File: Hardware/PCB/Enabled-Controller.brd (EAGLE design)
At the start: 54 x 71 mm, 14 parts, among them U1 ITSYBITSY

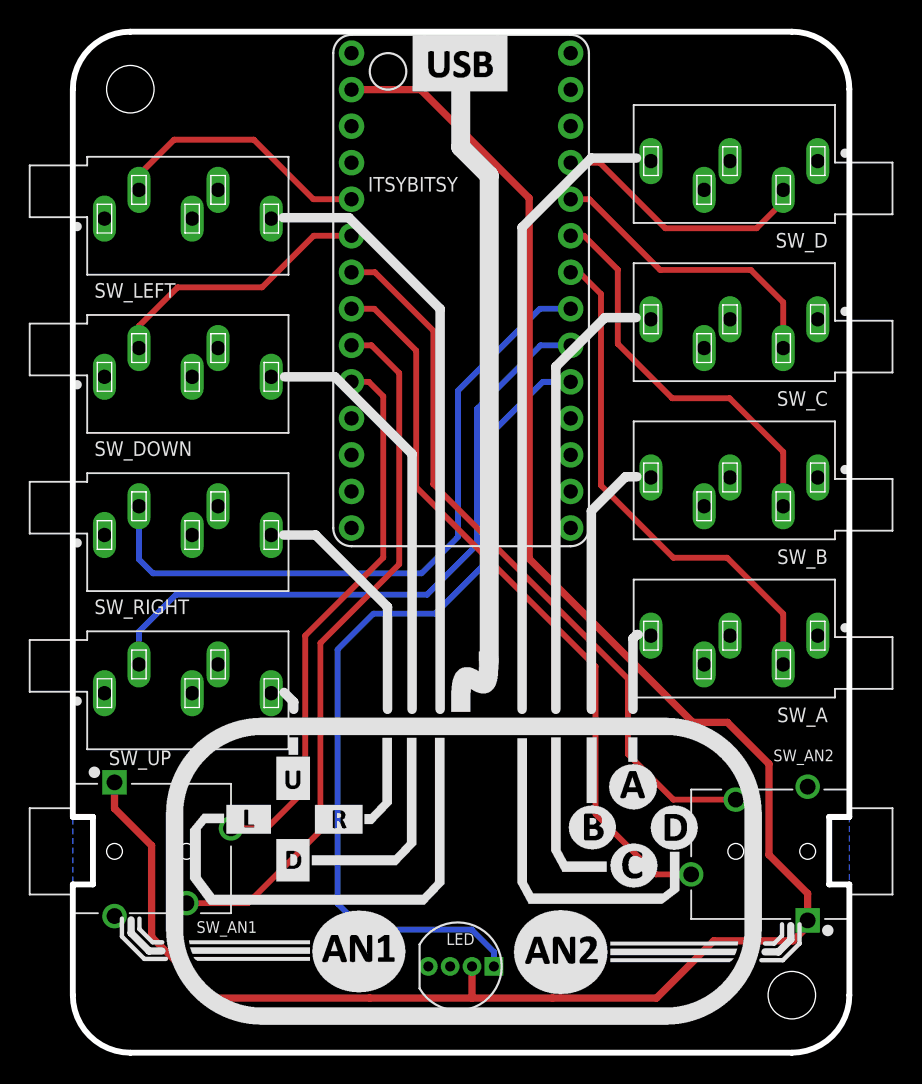
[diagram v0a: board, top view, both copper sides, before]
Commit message: Updated Eagle files
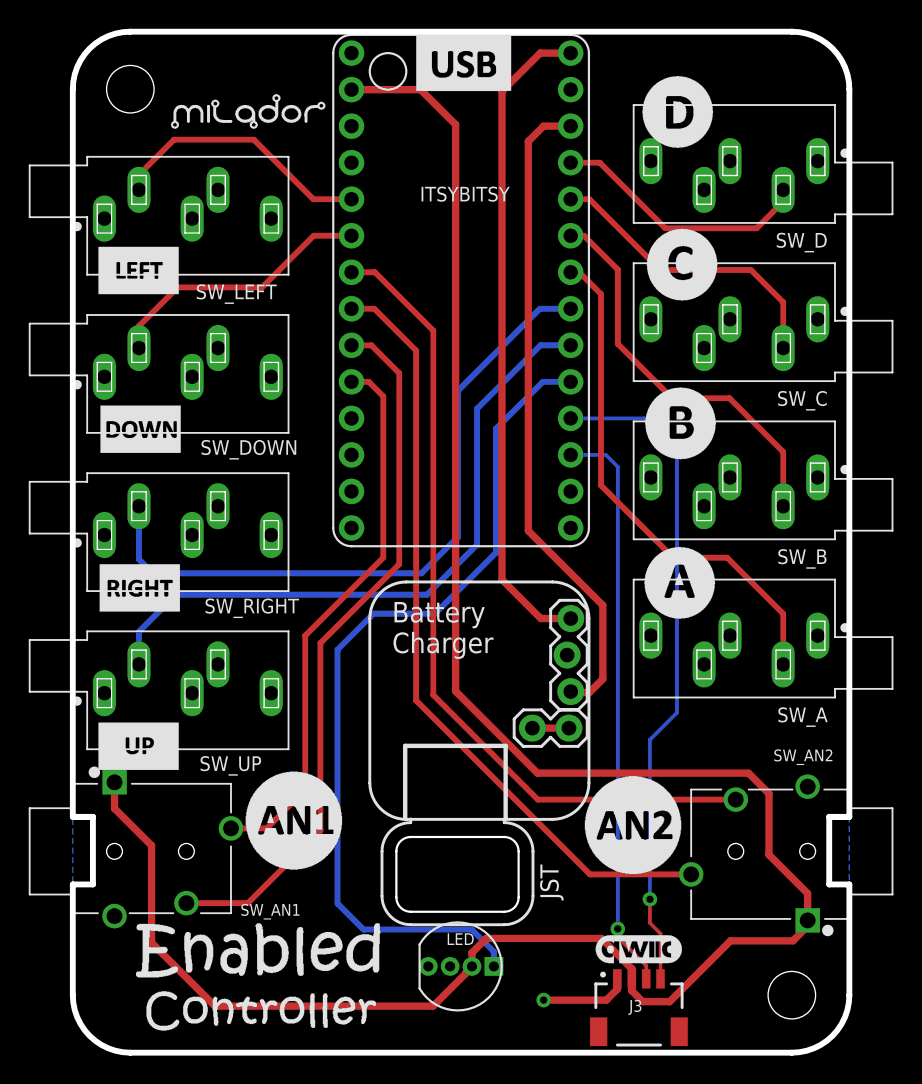
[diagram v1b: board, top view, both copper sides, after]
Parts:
- added J1: (no value), milador:HEADER_FEMALE-1X03_LONGER
- added J2: HEADER_FEMALE-1X2, milador:HEADER_FEMALE-1X02
- added J3: QWIIC, milador_SMD:CONNECTORS_JST04_1MM_RA
- added U$1: MILADOR-LOGO-, milador:MILADOR_LOGO1
- added U$21: (no value), SparkFun-Aesthetics:QWIIC_6MM
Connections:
- new net N$14: J3.4, U1.P_SCL
- new net N$15: J3.3, U1.P_SDA
- new net N$16: J1.3, U1.P_USB
- new net N$17: J1.1, U1.P_BAT
- new net N$18: J2.1, J2.2
- net +3V3: now also J3.2
- net GND: now also J3.1
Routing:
- net N$14: track 0.00 -> 46.1 mm, vias 0 -> 1
- net N$17: track 0.00 -> 45.7 mm
- net N$16: track 0.00 -> 45.6 mm
- net N$15: track 0.00 -> 40.0 mm, vias 0 -> 1
- net +3V3: track 139.0 -> 149.8 mm
- net GND: track 0.00 -> 6.16 mm, vias 0 -> 1
- net N$12: track 51.2 -> 56.8 mm
- net N$9: track 51.5 -> 54.2 mm
- net N$18: track 0.00 -> 2.54 mm
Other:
- outline, holes or cut-outs redrawn
- board text added: "Battery Charger"
- board text added: "JST"

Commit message: Added updated PCB files
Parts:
- removed J2: HEADER_FEMALE-1X2, milador:HEADER_FEMALE-1X02
- removed U$1: MILADOR-LOGO-, milador:MILADOR_LOGO1
- added LABEL1: MILADOR-LOGO-, milador:MILADOR_LOGO1
- renumbered U$21 to LABEL2
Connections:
- removed net N$18: J2.1, J2.2
- net GND: now also J1.2, SW_A.3, SW_B.3, SW_C.3, SW_D.3, SW_DOWN.3, SW_LEFT.3, SW_RIGHT.3, SW_UP.3
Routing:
- net N$18: track 2.54 -> 0.00 mm
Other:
- board text added: "V1.2"
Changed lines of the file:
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@@
 <drawing>
 <settings>
-<setting alwaysvectorfont="yes"/>
+<setting alwaysvectorfont="no"/>
 <setting keepoldvectorfont="yes"/>
 <setting verticaltext="up"/>
@@
 <layer number="20" name="Dimension" color="15" fill="1" visible="yes" active="yes"/>
 <layer number="21" name="tPlace" color="7" fill="1" visible="yes" active="yes"/>
-<layer number="22" name="bPlace" color="7" fill="1" visible="yes" active="yes"/>
+<layer number="22" name="bPlace" color="7" fill="1" visible="no" active="yes"/>
 <layer number="23" name="tOrigins" color="15" fill="1" visible="yes" active="yes"/>
 <layer number="24" name="bOrigins" color="15" fill="1" visible="yes" active="yes"/>
@@
 </layers>
 <board>
-<fusionsync huburn="a.cGVyc29uYWw6dWUyYWQxOTI2" projecturn="a.cGVyc29uYWw6dWUyYWQxOTI2IzIwMjAwODAxMzIwMTk3MTgx" f3durn="urn:adsk.wipprod:dm.lineage:0P3WCUaEQdKCa3VO5MvKcA" pcbguid="" lastpulledtime="" lastsyncedchangeguid="" latestrevisionid="d0e29ba4-d4c4-4277-8ff9-67c412f5de14" lastsyncedrevisionid="d0e29ba4-d4c4-4277-8ff9-67c412f5de14" lastboardhashguid="a98b978c-a84a-6d7b-aef6-eb2471a3cdfa" lastpushedtime="2021-06-05T22:54:26Z" linktopcb3d="true"/>
+<fusionsync huburn="a.cGVyc29uYWw6dWUyYWQxOTI2" projecturn="a.cGVyc29uYWw6dWUyYWQxOTI2IzIwMjAwODAxMzIwMTk3MTgx" f3durn="urn:adsk.wipprod:dm.lineage:0P3WCUaEQdKCa3VO5MvKcA" pcbguid="" lastpulledtime="" lastsyncedchangeguid="" latestrevisionid="83d8bdd9-ecd9-4150-ad09-6a1a40ea1fac" lastsyncedrevisionid="83d8bdd9-ecd9-4150-ad09-6a1a40ea1fac" lastboardhashguid="a26c7ad2-ae5e-e781-a83e-f818fcadd8db" lastpushedtime="2021-06-10T00:37:29Z" linktopcb3d="true"/>
 <plain>
 <wire x1="4" y1="0" x2="50" y2="0" width="0.4064" layer="20"/>
@@
 <wire x1="30" y1="16" x2="30" y2="16.25" width="0.2" layer="21"/>
 <text x="33.782" y="10.668" size="1.27" layer="21" rot="R90">JST</text>
+<text x="3.302" y="2.032" size="1.6764" layer="21" ratio="20" rot="R90">V1.2</text>
 </plain>
 <attributes>
@@
 </element>
 <element name="SW_AN1" library="MMC Eagle" library_urn="urn:adsk.eagle:library:13126479" package="CUI_SJ-43514" package3d_urn="urn:adsk.eagle:package:22282311/2" value="SJ-43514" x="5.5" y="14" smashed="yes">
-<attribute name="NAME" x="11.648" y="9.5238" size="0.8128" layer="25"/>
+<attribute name="NAME" x="11.648" y="10.7938" size="0.8128" layer="25"/>
 </element>
 <element name="SW_AN2" library="MMC Eagle" library_urn="urn:adsk.eagle:library:13126479" package="CUI_SJ-43514" package3d_urn="urn:adsk.eagle:package:22282311/2" value="SJ-43514" x="48.5" y="14" smashed="yes" rot="R180">
@@
 <attribute name="VALUE" x="32.468" y="31.46" size="0.6096" layer="27" font="vector" ratio="20" rot="R270"/>
 </element>
-<element name="J2" library="milador" library_urn="urn:adsk.eagle:library:12595918" package="HEADER_FEMALE-1X02" package3d_urn="urn:adsk.eagle:package:27250301/1" value="HEADER_FEMALE-1X2" x="31.96" y="22.57" smashed="yes"/>
-<element name="U$1" library="milador" library_urn="urn:adsk.eagle:library:12595918" package="MILADOR_LOGO1" package3d_urn="urn:adsk.eagle:package:28431737/1" value="MILADOR-LOGO-" x="12.319" y="64.2874" smashed="yes"/>
-<element name="U$21" library="SparkFun-Aesthetics" package="QWIIC_6MM" value="" x="39.3954" y="7.1882" smashed="yes"/>
+<element name="LABEL1" library="milador" library_urn="urn:adsk.eagle:library:12595918" package="MILADOR_LOGO1" package3d_urn="urn:adsk.eagle:package:28431737/1" value="MILADOR-LOGO-" x="12" y="64" smashed="yes"/>
+<element name="LABEL2" library="SparkFun-Aesthetics" package="QWIIC_6MM" value="" x="39.3954" y="7.1882" smashed="yes"/>
 </elements>
 <signals>
@@
 <wire x1="37.87" y1="4.4182" x2="37.87" y2="5.133340625" width="0.508" layer="1"/>
 <wire x1="37.1094" y1="3.6576" x2="37.87" y2="4.4182" width="0.508" layer="1"/>
+<contactref element="SW_UP" pad="3"/>
+<contactref element="SW_RIGHT" pad="3"/>
+<contactref element="SW_A" pad="3"/>
+<contactref element="SW_B" pad="3"/>
+<contactref element="SW_C" pad="3"/>
+<contactref element="SW_D" pad="3"/>
+<contactref element="SW_DOWN" pad="3"/>
+<contactref element="SW_LEFT" pad="3"/>
+<contactref element="J1" pad="2"/>
 </signal>
 <signal name="+3V3">
@@
 <wire x1="32.6851" y1="46.65" x2="34.62" y2="46.65" width="0.4064" layer="16"/>
 <wire x1="29.28" y1="6" x2="29.28" y2="7.02" width="0.4064" layer="16"/>
-<wire x1="29.28" y1="7.02" x2="27.74" y2="8.56" width="0.4064" layer="16"/>
-<wire x1="27.74" y1="8.56" x2="20.22" y2="8.56" width="0.4064" layer="16"/>
-<wire x1="20.22" y1="8.56" x2="18.41" y2="10.37" width="0.4064" layer="16"/>
+<wire x1="29.28" y1="7.02" x2="28.248" y2="8.052" width="0.4064" layer="16"/>
+<wire x1="28.248" y1="8.052" x2="20.728" y2="8.052" width="0.4064" layer="16"/>
+<wire x1="20.728" y1="8.052" x2="18.41" y2="10.37" width="0.4064" layer="16"/>
 <wire x1="29.43321875" y1="34.76945625" x2="29.43321875" y2="43.39811875" width="0.4064" layer="16"/>
 <wire x1="29.43321875" y1="43.39811875" x2="32.6851" y2="46.65" width="0.4064" layer="16"/>
@@
 <wire x1="29.845" y1="32.893" x2="32.548" y2="30.19" width="0.508" layer="1"/>
 </signal>
-<signal name="N$18">
-<contactref element="J2" pad="2"/>
-<contactref element="J2" pad="1"/>
-<wire x1="34.5" y1="22.57" x2="31.96" y2="22.57" width="0.508" layer="1"/>
-</signal>
 </signals>
